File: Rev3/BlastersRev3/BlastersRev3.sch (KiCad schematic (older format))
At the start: 64 parts, among them SW1 Switch, SW10 Switch, SW11 Switch, SW12 Switch, SW13 Switch, SW14 Switch, SW15 Switch, SW16 Switch, SW17 Switch, SW18 Switch, SW19 Switch, SW2 Switch, SW20 Switch, SW21 Switch, SW22 Switch, SW23 Switch, SW24 Switch, SW25 Switch, SW26 Switch, SW27 Switch, SW28 Switch, SW29 Switch, SW3 Switch, SW30 Switch, SW4 Switch, SW5 Switch, SW6 Switch, SW7 Switch, SW8 Switch, SW9 Switch, U1 ProMicro

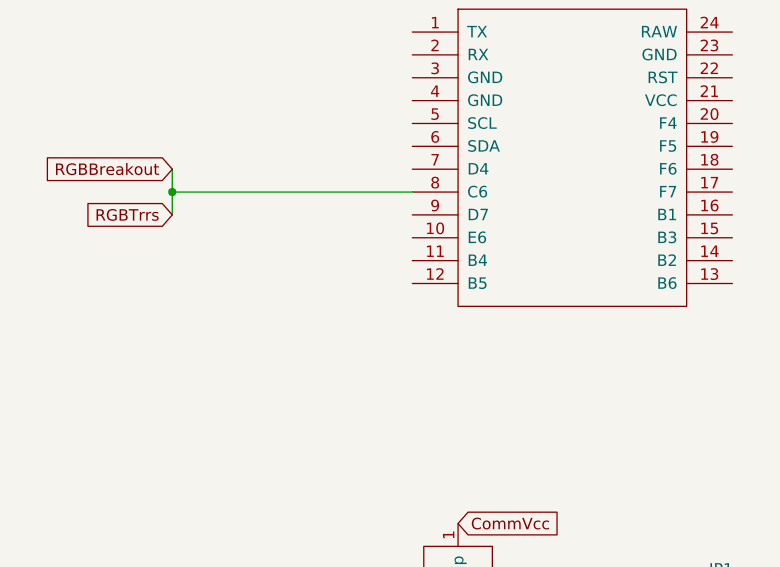
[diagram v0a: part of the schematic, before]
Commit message: Preliminary col routing done
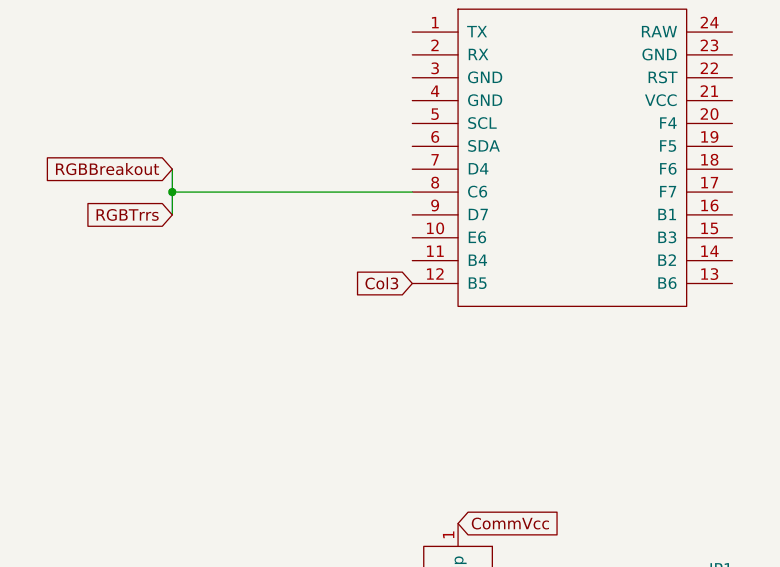
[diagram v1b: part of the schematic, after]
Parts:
- SW1, SW10, SW11, SW12, SW13, SW14, SW15, SW16, SW17, SW18, SW19, SW2, SW20, SW21, SW22, SW23, SW24, SW25, SW26, SW27, SW28, SW29, SW3, SW30, SW4, SW5, SW6, SW7, SW8, SW9: footprint KeyboardFootprints:MX_Switch_Symmetric -> KeyboardFootprints:MX_Removable
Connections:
- net Col3: now also U1.12 (B5)
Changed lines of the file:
@@
 EESchema Schematic File Version 4
+LIBS:BlastersRev3-cache
 EELAYER 29 0
 EELAYER END
@@
 F 0 "SW1" H 5608 2473 50  0000 C CNN
 F 1 "Switch" H 5600 2250 50  0001 C CNN
-F 2 "KeyboardFootprints:MX_Switch_Symmetric" H 5650 2200 50  0001 C CNN
+F 2 "KeyboardFootprints:MX_Removable" H 5650 2200 50  0001 C CNN
 F 3 "" H 5650 2200 50  0001 C CNN
 	1    5650 2200
@@
 F 0 "SW5" H 6008 2473 50  0000 C CNN
 F 1 "Switch" H 6000 2250 50  0001 C CNN
-F 2 "KeyboardFootprints:MX_Switch_Symmetric" H 6050 2200 50  0001 C CNN
+F 2 "KeyboardFootprints:MX_Removable" H 6050 2200 50  0001 C CNN
 F 3 "" H 6050 2200 50  0001 C CNN
 	1    6050 2200
@@
 F 0 "SW9" H 6408 2473 50  0000 C CNN
 F 1 "Switch" H 6400 2250 50  0001 C CNN
-F 2 "KeyboardFootprints:MX_Switch_Symmetric" H 6450 2200 50  0001 C CNN
+F 2 "KeyboardFootprints:MX_Removable" H 6450 2200 50  0001 C CNN
 F 3 "" H 6450 2200 50  0001 C CNN
 	1    6450 2200
@@
 F 0 "SW13" H 6808 2473 50  0000 C CNN
 F 1 "Switch" H 6800 2250 50  0001 C CNN
-F 2 "KeyboardFootprints:MX_Switch_Symmetric" H 6850 2200 50  0001 C CNN
+F 2 "KeyboardFootprints:MX_Removable" H 6850 2200 50  0001 C CNN
 F 3 "" H 6850 2200 50  0001 C CNN
 	1    6850 2200
@@
 F 0 "SW17" H 7208 2473 50  0000 C CNN
 F 1 "Switch" H 7200 2250 50  0001 C CNN
-F 2 "KeyboardFootprints:MX_Switch_Symmetric" H 7250 2200 50  0001 C CNN
+F 2 "KeyboardFootprints:MX_Removable" H 7250 2200 50  0001 C CNN
 F 3 "" H 7250 2200 50  0001 C CNN
 	1    7250 2200
@@
 F 0 "SW21" H 7608 2473 50  0000 C CNN
 F 1 "Switch" H 7600 2250 50  0001 C CNN
-F 2 "KeyboardFootprints:MX_Switch_Symmetric" H 7650 2200 50  0001 C CNN
+F 2 "KeyboardFootprints:MX_Removable" H 7650 2200 50  0001 C CNN
 F 3 "" H 7650 2200 50  0001 C CNN
 	1    7650 2200
@@
 F 0 "SW26" H 8008 2473 50  0000 C CNN
 F 1 "Switch" H 8000 2250 50  0001 C CNN
-F 2 "KeyboardFootprints:MX_Switch_Symmetric" H 8050 2200 50  0001 C CNN
+F 2 "KeyboardFootprints:MX_Removable" H 8050 2200 50  0001 C CNN
 F 3 "" H 8050 2200 50  0001 C CNN
 	1    8050 2200
@@
 F 0 "SW2" H 5608 3073 50  0000 C CNN
 F 1 "Switch" H 5600 2850 50  0001 C CNN
-F 2 "KeyboardFootprints:MX_Switch_Symmetric" H 5650 2800 50  0001 C CNN
+F 2 "KeyboardFootprints:MX_Removable" H 5650 2800 50  0001 C CNN
 F 3 "" H 5650 2800 50  0001 C CNN
 	1    5650 2800
@@
 F 0 "SW6" H 6008 3073 50  0000 C CNN
 F 1 "Switch" H 6000 2850 50  0001 C CNN
-F 2 "KeyboardFootprints:MX_Switch_Symmetric" H 6050 2800 50  0001 C CNN
+F 2 "KeyboardFootprints:MX_Removable" H 6050 2800 50  0001 C CNN
 F 3 "" H 6050 2800 50  0001 C CNN
 	1    6050 2800
@@
 F 0 "SW10" H 6408 3073 50  0000 C CNN
 F 1 "Switch" H 6400 2850 50  0001 C CNN
-F 2 "KeyboardFootprints:MX_Switch_Symmetric" H 6450 2800 50  0001 C CNN
+F 2 "KeyboardFootprints:MX_Removable" H 6450 2800 50  0001 C CNN
 F 3 "" H 6450 2800 50  0001 C CNN
 	1    6450 2800
@@
 F 0 "SW14" H 6808 3073 50  0000 C CNN
 F 1 "Switch" H 6800 2850 50  0001 C CNN
-F 2 "KeyboardFootprints:MX_Switch_Symmetric" H 6850 2800 50  0001 C CNN
+F 2 "KeyboardFootprints:MX_Removable" H 6850 2800 50  0001 C CNN
 F 3 "" H 6850 2800 50  0001 C CNN
 	1    6850 2800
@@
 F 0 "SW18" H 7208 3073 50  0000 C CNN
 F 1 "Switch" H 7200 2850 50  0001 C CNN
-F 2 "KeyboardFootprints:MX_Switch_Symmetric" H 7250 2800 50  0001 C CNN
+F 2 "KeyboardFootprints:MX_Removable" H 7250 2800 50  0001 C CNN
 F 3 "" H 7250 2800 50  0001 C CNN
 	1    7250 2800
@@
 F 0 "SW22" H 7608 3073 50  0000 C CNN
 F 1 "Switch" H 7600 2850 50  0001 C CNN
-F 2 "KeyboardFootprints:MX_Switch_Symmetric" H 7650 2800 50  0001 C CNN
+F 2 "KeyboardFootprints:MX_Removable" H 7650 2800 50  0001 C CNN
 F 3 "" H 7650 2800 50  0001 C CNN
 	1    7650 2800
@@
 F 0 "SW27" H 8008 3073 50  0000 C CNN
 F 1 "Switch" H 8000 2850 50  0001 C CNN
-F 2 "KeyboardFootprints:MX_Switch_Symmetric" H 8050 2800 50  0001 C CNN
+F 2 "KeyboardFootprints:MX_Removable" H 8050 2800 50  0001 C CNN
 F 3 "" H 8050 2800 50  0001 C CNN
 	1    8050 2800
@@
 F 0 "SW3" H 5608 3673 50  0000 C CNN
 F 1 "Switch" H 5600 3450 50  0001 C CNN
-F 2 "KeyboardFootprints:MX_Switch_Symmetric" H 5650 3400 50  0001 C CNN
+F 2 "KeyboardFootprints:MX_Removable" H 5650 3400 50  0001 C CNN
 F 3 "" H 5650 3400 50  0001 C CNN
 	1    5650 3400
@@
 F 0 "SW7" H 6008 3673 50  0000 C CNN
 F 1 "Switch" H 6000 3450 50  0001 C CNN
-F 2 "KeyboardFootprints:MX_Switch_Symmetric" H 6050 3400 50  0001 C CNN
+F 2 "KeyboardFootprints:MX_Removable" H 6050 3400 50  0001 C CNN
 F 3 "" H 6050 3400 50  0001 C CNN
 	1    6050 3400
@@
 F 0 "SW11" H 6408 3673 50  0000 C CNN
 F 1 "Switch" H 6400 3450 50  0001 C CNN
-F 2 "KeyboardFootprints:MX_Switch_Symmetric" H 6450 3400 50  0001 C CNN
+F 2 "KeyboardFootprints:MX_Removable" H 6450 3400 50  0001 C CNN
 F 3 "" H 6450 3400 50  0001 C CNN
 	1    6450 3400
@@
 F 0 "SW15" H 6808 3673 50  0000 C CNN
 F 1 "Switch" H 6800 3450 50  0001 C CNN
-F 2 "KeyboardFootprints:MX_Switch_Symmetric" H 6850 3400 50  0001 C CNN
+F 2 "KeyboardFootprints:MX_Removable" H 6850 3400 50  0001 C CNN
 F 3 "" H 6850 3400 50  0001 C CNN
 	1    6850 3400
@@
 F 0 "SW19" H 7208 3673 50  0000 C CNN
 F 1 "Switch" H 7200 3450 50  0001 C CNN
-F 2 "KeyboardFootprints:MX_Switch_Symmetric" H 7250 3400 50  0001 C CNN
+F 2 "KeyboardFootprints:MX_Removable" H 7250 3400 50  0001 C CNN
 F 3 "" H 7250 3400 50  0001 C CNN
 	1    7250 3400
@@
 F 0 "SW23" H 7608 3673 50  0000 C CNN
 F 1 "Switch" H 7600 3450 50  0001 C CNN
-F 2 "KeyboardFootprints:MX_Switch_Symmetric" H 7650 3400 50  0001 C CNN
+F 2 "KeyboardFootprints:MX_Removable" H 7650 3400 50  0001 C CNN
 F 3 "" H 7650 3400 50  0001 C CNN
 	1    7650 3400
@@
 F 0 "SW28" H 8008 3673 50  0000 C CNN
 F 1 "Switch" H 8000 3450 50  0001 C CNN
-F 2 "KeyboardFootprints:MX_Switch_Symmetric" H 8050 3400 50  0001 C CNN
+F 2 "KeyboardFootprints:MX_Removable" H 8050 3400 50  0001 C CNN
 F 3 "" H 8050 3400 50  0001 C CNN
 	1    8050 3400
@@
 F 0 "SW4" H 5608 4273 50  0000 C CNN
 F 1 "Switch" H 5600 4050 50  0001 C CNN
-F 2 "KeyboardFootprints:MX_Switch_Symmetric" H 5650 4000 50  0001 C CNN
+F 2 "KeyboardFootprints:MX_Removable" H 5650 4000 50  0001 C CNN
 F 3 "" H 5650 4000 50  0001 C CNN
 	1    5650 4000
@@
 F 0 "SW8" H 6008 4273 50  0000 C CNN
 F 1 "Switch" H 6000 4050 50  0001 C CNN
-F 2 "KeyboardFootprints:MX_Switch_Symmetric" H 6050 4000 50  0001 C CNN
+F 2 "KeyboardFootprints:MX_Removable" H 6050 4000 50  0001 C CNN
 F 3 "" H 6050 4000 50  0001 C CNN
 	1    6050 4000
@@
 F 0 "SW12" H 6408 4273 50  0000 C CNN
 F 1 "Switch" H 6400 4050 50  0001 C CNN
-F 2 "KeyboardFootprints:MX_Switch_Symmetric" H 6450 4000 50  0001 C CNN
+F 2 "KeyboardFootprints:MX_Removable" H 6450 4000 50  0001 C CNN
 F 3 "" H 6450 4000 50  0001 C CNN
 	1    6450 4000
@@
 F 0 "SW16" H 6808 4273 50  0000 C CNN
 F 1 "Switch" H 6800 4050 50  0001 C CNN
-F 2 "KeyboardFootprints:MX_Switch_Symmetric" H 6850 4000 50  0001 C CNN
+F 2 "KeyboardFootprints:MX_Removable" H 6850 4000 50  0001 C CNN
 F 3 "" H 6850 4000 50  0001 C CNN
 	1    6850 4000
@@
 F 0 "SW20" H 7208 4273 50  0000 C CNN
 F 1 "Switch" H 7200 4050 50  0001 C CNN
-F 2 "KeyboardFootprints:MX_Switch_Symmetric" H 7250 4000 50  0001 C CNN
+F 2 "KeyboardFootprints:MX_Removable" H 7250 4000 50  0001 C CNN
 F 3 "" H 7250 4000 50  0001 C CNN
 	1    7250 4000
@@
 F 0 "SW24" H 7608 4273 50  0000 C CNN
 F 1 "Switch" H 7600 4050 50  0001 C CNN
-F 2 "KeyboardFootprints:MX_Switch_Symmetric" H 7650 4000 50  0001 C CNN
+F 2 "KeyboardFootprints:MX_Removable" H 7650 4000 50  0001 C CNN
 F 3 "" H 7650 4000 50  0001 C CNN
 	1    7650 4000
@@
 F 0 "SW29" H 8008 4273 50  0000 C CNN
 F 1 "Switch" H 8000 4050 50  0001 C CNN
-F 2 "KeyboardFootprints:MX_Switch_Symmetric" H 8050 4000 50  0001 C CNN
+F 2 "KeyboardFootprints:MX_Removable" H 8050 4000 50  0001 C CNN
 F 3 "" H 8050 4000 50  0001 C CNN
 	1    8050 4000
@@
 F 0 "SW25" H 7608 4873 50  0000 C CNN
 F 1 "Switch" H 7600 4650 50  0001 C CNN
-F 2 "KeyboardFootprints:MX_Switch_Symmetric" H 7650 4600 50  0001 C CNN
+F 2 "KeyboardFootprints:MX_Removable" H 7650 4600 50  0001 C CNN
 F 3 "" H 7650 4600 50  0001 C CNN
 	1    7650 4600
@@
 F 0 "SW30" H 8008 4873 50  0000 C CNN
 F 1 "Switch" H 8000 4650 50  0001 C CNN
-F 2 "KeyboardFootprints:MX_Switch_Symmetric" H 8050 4600 50  0001 C CNN
+F 2 "KeyboardFootprints:MX_Removable" H 8050 4600 50  0001 C CNN
 F 3 "" H 8050 4600 50  0001 C CNN
 	1    8050 4600
@@
 Text GLabel 8150 1800 0    50   Input ~ 0
 Col6
+Text GLabel 2500 3250 0    50   Input ~ 0
+Col3
 $EndSCHEMATC
